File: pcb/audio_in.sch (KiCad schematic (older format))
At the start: 18 parts, among them U7 MCP6409

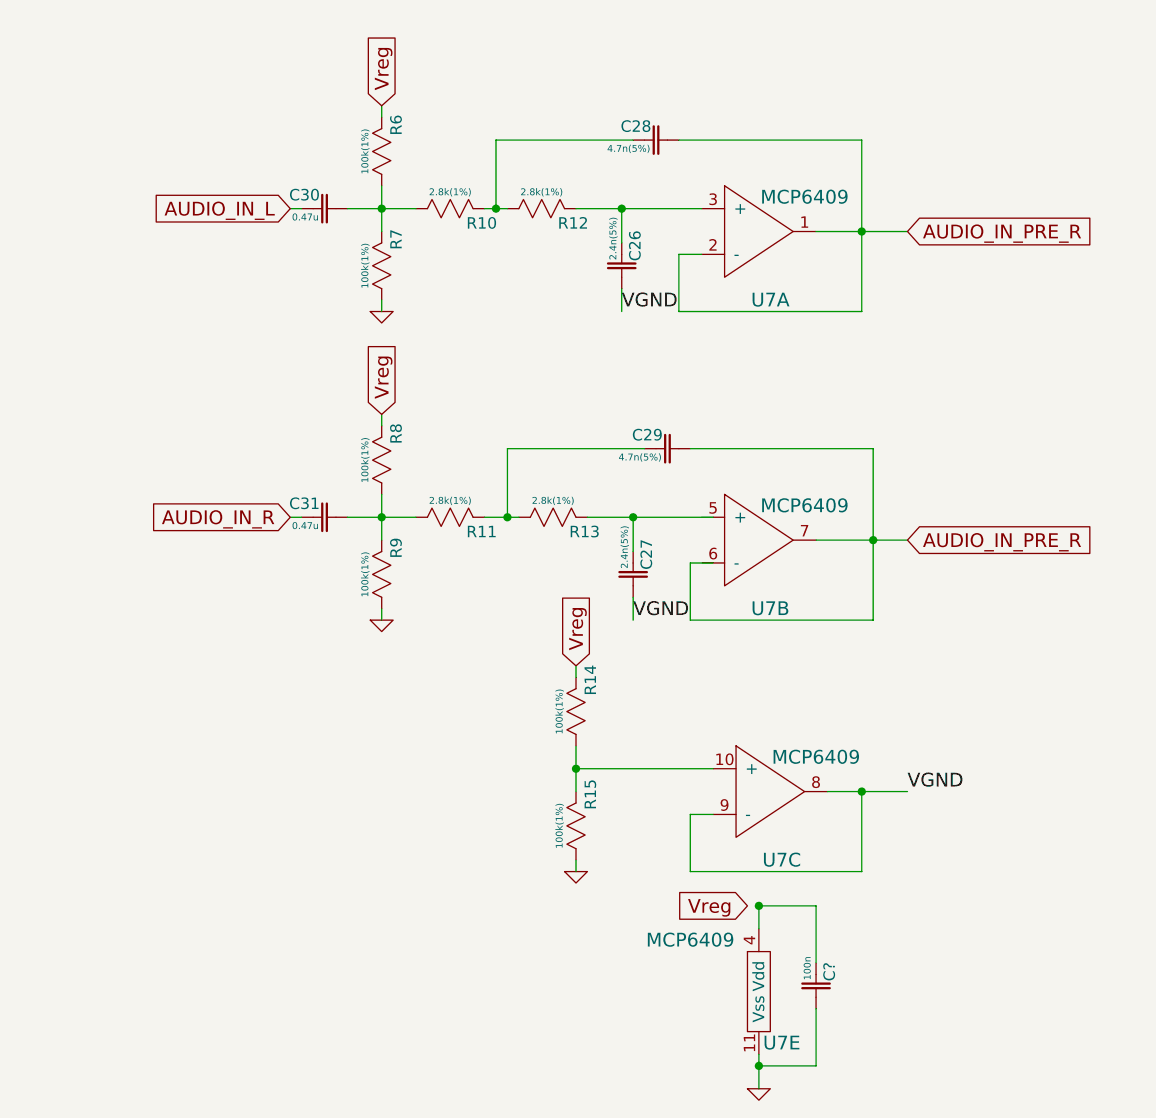
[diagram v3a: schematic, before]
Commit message: Added TRS audio connector
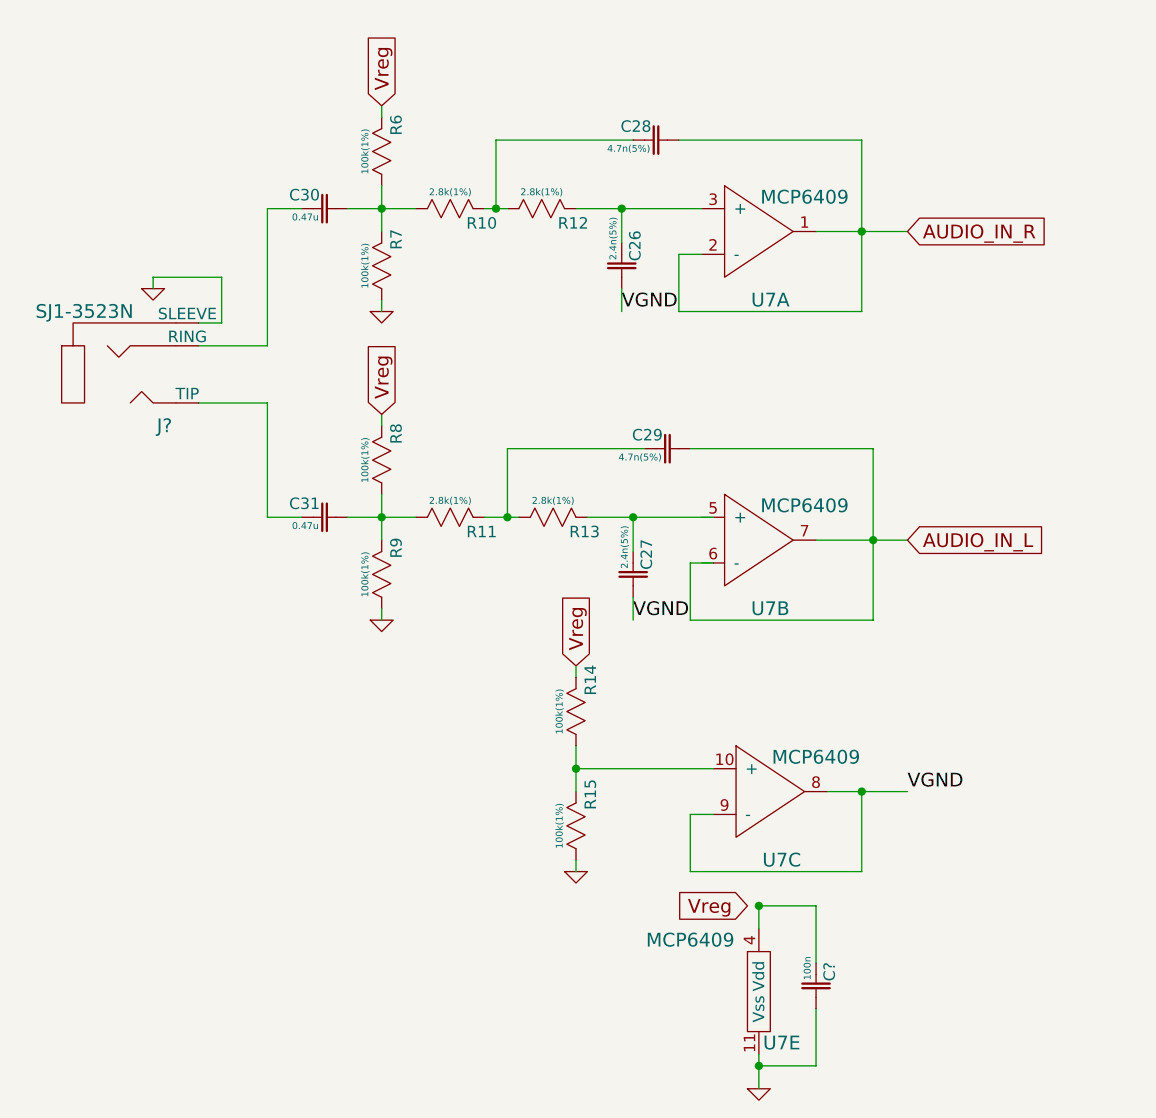
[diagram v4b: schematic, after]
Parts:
- added J?: SJ1-3523N, symbol TRS_CONN
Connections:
- net labels removed: AUDIO_IN_PRE_R
- wire segments 49 -> 57
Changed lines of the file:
@@
-EESchema Schematic File Version 2  date Thu 26 Jul 2012 02:13:26 PM EDT
+EESchema Schematic File Version 2  date Thu 26 Jul 2012 02:28:43 PM EDT
 LIBS:power
 LIBS:device
@@
 $EndDescr
 Wire Wire Line
+	1700 4000 1550 4000
+Wire Wire Line
+	1550 4000 1550 3500
+Wire Wire Line
+	1550 3500 1250 3500
+Wire Wire Line
+	1250 3150 1350 3150
+Wire Wire Line
+	1350 3150 1350 2950
+Wire Wire Line
+	1350 2950 1050 2950
+Wire Wire Line
+	1050 2950 1050 3000
+Wire Wire Line
+	3700 6400 3950 6400
+Connection ~ 3700 6400
+Wire Wire Line
+	3950 6400 3950 6150
+Connection ~ 3700 5700
+Wire Wire Line
+	3950 5950 3950 5700
+Wire Wire Line
+	1900 4000 2200 4000
+Wire Wire Line
+	2050 3550 2050 3600
+Wire Wire Line
+	2050 4450 2050 4400
+Connection ~ 2050 4000
+Wire Wire Line
+	2050 3900 2050 4100
+Wire Wire Line
+	3150 4350 3150 4450
+Wire Wire Line
+	3100 3100 3100 3000
+Connection ~ 4150 5200
+Wire Wire Line
+	4000 5200 4350 5200
+Wire Wire Line
+	4150 5200 4150 5550
+Wire Wire Line
+	4150 5550 3400 5550
+Wire Wire Line
+	3400 5550 3400 5300
+Wire Wire Line
+	3400 5300 3500 5300
+Wire Wire Line
+	2900 4650 2900 4700
+Connection ~ 4200 4100
+Wire Wire Line
+	3950 4100 4350 4100
+Wire Wire Line
+	4200 4450 4200 3700
+Wire Wire Line
+	4200 4450 3400 4450
+Wire Wire Line
+	3400 4450 3400 4200
+Wire Wire Line
+	3400 4200 3500 4200
+Wire Wire Line
+	2900 5550 2900 5500
+Connection ~ 2600 4000
+Wire Wire Line
+	2500 4000 2650 4000
+Connection ~ 3150 4000
+Wire Wire Line
+	3150 4000 3150 4150
+Wire Wire Line
+	2950 4000 3500 4000
+Wire Wire Line
+	4200 3700 3400 3700
+Wire Wire Line
+	3200 3700 2600 3700
+Wire Wire Line
+	2600 3700 2600 4000
+Connection ~ 2900 5100
+Wire Wire Line
+	2900 5100 3500 5100
+Wire Wire Line
+	2900 5000 2900 5200
+Connection ~ 4150 2750
+Wire Wire Line
+	3350 3100 4150 3100
+Wire Wire Line
+	3350 3100 3350 2850
+Wire Wire Line
+	3350 2850 3450 2850
+Wire Wire Line
+	2050 3100 2050 3050
+Connection ~ 2550 2650
+Wire Wire Line
+	2500 2650 2600 2650
+Connection ~ 3100 2650
+Wire Wire Line
+	3100 2650 3100 2800
+Wire Wire Line
+	2900 2650 3450 2650
+Wire Wire Line
+	3950 2750 4350 2750
+Wire Wire Line
+	4150 3100 4150 2350
+Wire Wire Line
+	4150 2350 3350 2350
+Wire Wire Line
+	3150 2350 2550 2350
+Wire Wire Line
+	2550 2350 2550 2650
+Wire Wire Line
+	2050 2200 2050 2250
+Connection ~ 2050 2650
+Wire Wire Line
+	1900 2650 2200 2650
+Wire Wire Line
+	2050 2550 2050 2750
+Wire Wire Line
+	3700 6500 3700 6350
+Wire Wire Line
+	3700 5800 3700 5700
+Wire Wire Line
 	3700 5700 3950 5700
 Wire Wire Line
-	3700 5700 3700 5800
-Wire Wire Line
-	3700 6500 3700 6350
-Wire Wire Line
-	2050 2550 2050 2750
-Wire Wire Line
-	1900 2650 2200 2650
-Connection ~ 2050 2650
-Wire Wire Line
-	2050 2200 2050 2250
-Wire Wire Line
-	2550 2650 2550 2350
-Wire Wire Line
-	2550 2350 3150 2350
-Wire Wire Line
-	3350 2350 4150 2350
-Wire Wire Line
-	4150 2350 4150 3100
-Wire Wire Line
-	3950 2750 4350 2750
-Wire Wire Line
-	2900 2650 3450 2650
-Wire Wire Line
-	3100 2650 3100 2800
-Connection ~ 3100 2650
-Wire Wire Line
-	2500 2650 2600 2650
-Connection ~ 2550 2650
-Wire Wire Line
-	2050 3100 2050 3050
-Wire Wire Line
-	3450 2850 3350 2850
-Wire Wire Line
-	3350 2850 3350 3100
-Wire Wire Line
-	3350 3100 4150 3100
-Connection ~ 4150 2750
-Wire Wire Line
-	2900 5000 2900 5200
-Wire Wire Line
-	2900 5100 3500 5100
-Connection ~ 2900 5100
-Wire Wire Line
-	2600 4000 2600 3700
-Wire Wire Line
-	2600 3700 3200 3700
-Wire Wire Line
-	3400 3700 4200 3700
-Wire Wire Line
-	2950 4000 3500 4000
-Wire Wire Line
-	3150 4000 3150 4150
-Connection ~ 3150 4000
-Wire Wire Line
-	2500 4000 2650 4000
-Connection ~ 2600 4000
-Wire Wire Line
-	2900 5550 2900 5500
-Wire Wire Line
-	3500 4200 3400 4200
-Wire Wire Line
-	3400 4200 3400 4450
-Wire Wire Line
-	3400 4450 4200 4450
-Wire Wire Line
-	4200 4450 4200 3700
-Wire Wire Line
-	3950 4100 4350 4100
-Connection ~ 4200 4100
-Wire Wire Line
-	2900 4650 2900 4700
-Wire Wire Line
-	3500 5300 3400 5300
-Wire Wire Line
-	3400 5300 3400 5550
-Wire Wire Line
-	3400 5550 4150 5550
-Wire Wire Line
-	4150 5550 4150 5200
-Wire Wire Line
-	4000 5200 4350 5200
-Connection ~ 4150 5200
-Wire Wire Line
-	3100 3100 3100 3000
-Wire Wire Line
-	3150 4350 3150 4450
-Wire Wire Line
-	2050 3900 2050 4100
-Connection ~ 2050 4000
-Wire Wire Line
-	2050 4450 2050 4400
-Wire Wire Line
-	2050 3550 2050 3600
-Wire Wire Line
-	1900 4000 2200 4000
-Wire Wire Line
-	1650 2650 1700 2650
-Wire Wire Line
-	1700 4000 1650 4000
-Wire Wire Line
-	3950 5700 3950 5950
-Connection ~ 3700 5700
-Wire Wire Line
-	3950 6150 3950 6400
-Connection ~ 3700 6400
-Wire Wire Line
-	3950 6400 3700 6400
+	1250 3250 1550 3250
+Wire Wire Line
+	1550 3250 1550 2650
+Wire Wire Line
+	1550 2650 1700 2650
+$Comp
+L GND #PWR?
+U 1 1 50118BD6
+P 1050 3000
+F 0 "#PWR?" H 1050 3000 30  0001 C CNN
+F 1 "GND" H 1050 2930 30  0001 C CNN
+	1    1050 3000
+	1    0    0    -1
+$EndComp
+$Comp
+L TRS_CONN J?
+U 1 1 50118BBE
+P 800 3350
+F 0 "J?" H 1100 3100 60  0000 C CNN
+F 1 "SJ1-3523N" H 750 3600 60  0000 C CNN
+	1    800  3350
+	1    0    0    -1
+$EndComp
 $Comp
 L CAP C?
@@
 	1    0    0    -1
 $EndComp
-Text GLabel 1650 2650 0    60   Input ~ 0
+Text GLabel 4350 4100 2    60   Input ~ 0
 AUDIO_IN_L
-Text GLabel 1650 4000 0    60   Input ~ 0
+Text GLabel 4350 2750 2    60   Input ~ 0
 AUDIO_IN_R
-Text GLabel 4350 4100 2    60   Input ~ 0
-AUDIO_IN_PRE_R
-Text GLabel 4350 2750 2    60   Input ~ 0
-AUDIO_IN_PRE_R
 $Comp
 L CAP C30

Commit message: Added LCD and started wiring busses
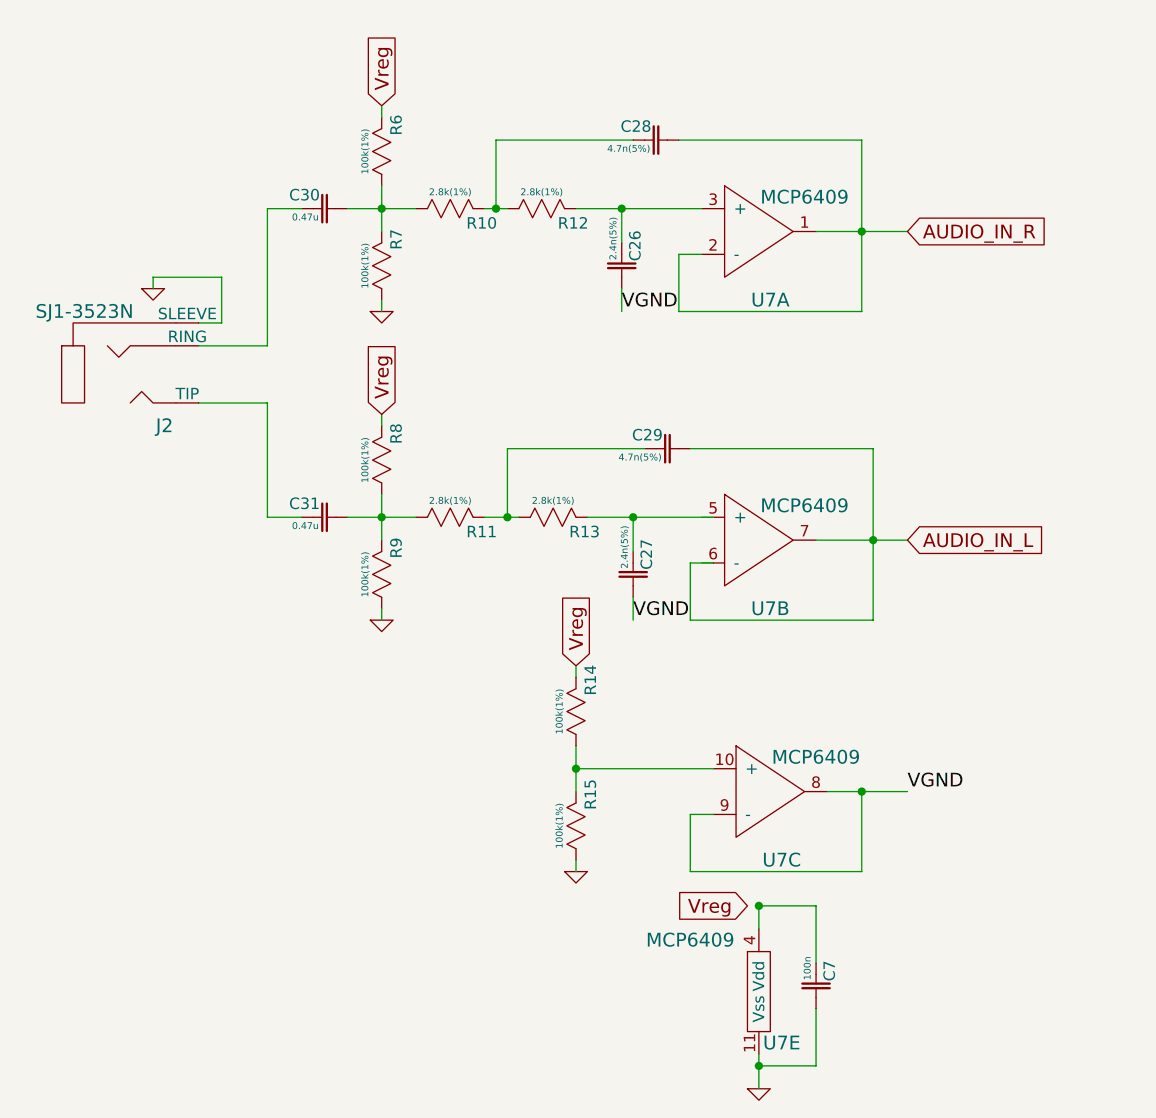
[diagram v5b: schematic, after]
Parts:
- gave numbers to parts that had none: 2
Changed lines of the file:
@@
-EESchema Schematic File Version 2  date Thu 26 Jul 2012 02:28:43 PM EDT
+EESchema Schematic File Version 2  date Thu 26 Jul 2012 11:54:13 PM EDT
 LIBS:power
 LIBS:device
@@
 EELAYER 25  0
 EELAYER END
-$Descr A4 11700 8267
+$Descr A4 11693 8268
 encoding utf-8
 Sheet 5 5
 Title ""
-Date "26 jul 2012"
+Date "27 jul 2012"
 Rev ""
 Comp ""
@@
 	1550 2650 1700 2650
 $Comp
-L GND #PWR?
+L GND #PWR24
 U 1 1 50118BD6
 P 1050 3000
-F 0 "#PWR?" H 1050 3000 30  0001 C CNN
+F 0 "#PWR24" H 1050 3000 30  0001 C CNN
 F 1 "GND" H 1050 2930 30  0001 C CNN
 	1    1050 3000
@@
 $EndComp
 $Comp
-L TRS_CONN J?
+L TRS_CONN J2
 U 1 1 50118BBE
 P 800 3350
-F 0 "J?" H 1100 3100 60  0000 C CNN
+F 0 "J2" H 1100 3100 60  0000 C CNN
 F 1 "SJ1-3523N" H 750 3600 60  0000 C CNN
 	1    800  3350
@@
 $EndComp
 $Comp
-L CAP C?
+L CAP C7
 U 1 1 50118878
 P 3950 6050
-F 0 "C?" H 3970 6020 50  0000 L TNN
+F 0 "C7" H 3970 6020 50  0000 L TNN
 F 1 "100n" H 3975 6070 30  0000 L BNN
 	1    3950 6050
@@
 Vreg
 $Comp
-L GND #PWR25
+L GND #PWR28
 U 1 1 5010D90D
 P 3700 6500
-F 0 "#PWR25" H 3700 6500 30  0001 C CNN
+F 0 "#PWR28" H 3700 6500 30  0001 C CNN
 F 1 "GND" H 3700 6430 30  0001 C CNN
 	1    3700 6500
@@
 Vreg
 $Comp
-L GND #PWR22
+L GND #PWR25
 U 1 1 5010D9BD
 P 2050 3100
-F 0 "#PWR22" H 2050 3100 30  0001 C CNN
+F 0 "#PWR25" H 2050 3100 30  0001 C CNN
 F 1 "GND" H 2050 3030 30  0001 C CNN
 	1    2050 3100
@@
 Vreg
 $Comp
-L GND #PWR24
+L GND #PWR27
 U 1 1 5010DA28
 P 2900 5550
-F 0 "#PWR24" H 2900 5550 30  0001 C CNN
+F 0 "#PWR27" H 2900 5550 30  0001 C CNN
 F 1 "GND" H 2900 5480 30  0001 C CNN
 	1    2900 5550
@@
 Vreg
 $Comp
-L GND #PWR23
+L GND #PWR26
 U 1 1 5010DC3F
 P 2050 4450
-F 0 "#PWR23" H 2050 4450 30  0001 C CNN
+F 0 "#PWR26" H 2050 4450 30  0001 C CNN
 F 1 "GND" H 2050 4380 30  0001 C CNN
 	1    2050 4450

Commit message: Broke up schematic in a more modular fashion -- Added LCD footprint
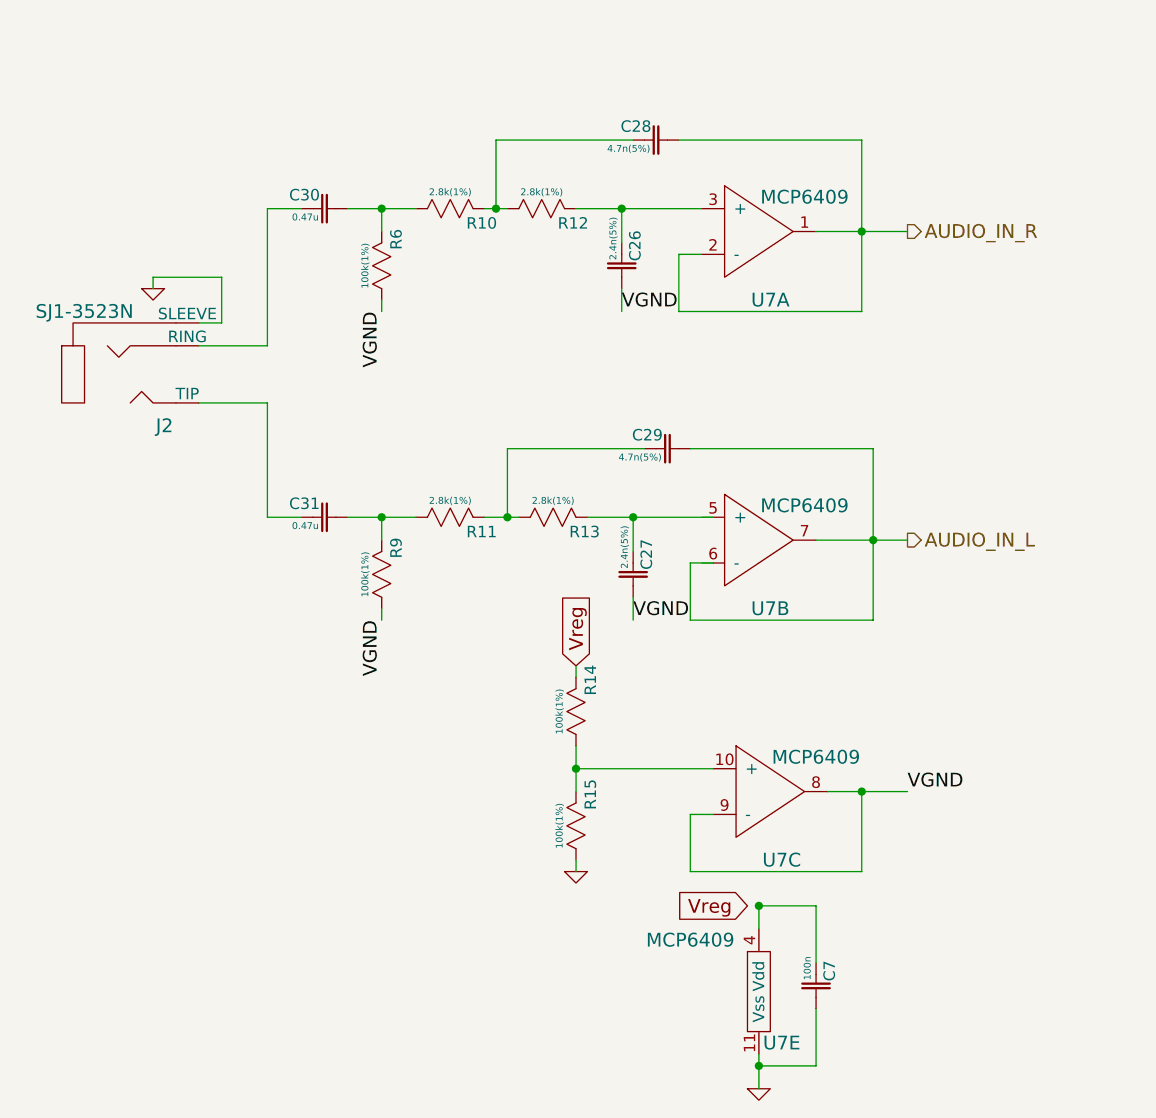
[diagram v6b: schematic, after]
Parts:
- removed R7, R8: 100k(1%), symbol RES
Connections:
- wire segments 57 -> 55
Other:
- moved on the sheet: R6
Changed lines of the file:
@@
-EESchema Schematic File Version 2  date Thu 26 Jul 2012 11:54:13 PM EDT
+EESchema Schematic File Version 2  date Tue 31 Jul 2012 10:29:35 PM EDT
 LIBS:power
 LIBS:device
@@
 EELAYER 25  0
 EELAYER END
-$Descr A4 11693 8268
+$Descr A4 11700 8267
 encoding utf-8
-Sheet 5 5
+Sheet 6 6
 Title ""
-Date "27 jul 2012"
+Date "1 aug 2012"
 Rev ""
 Comp ""
@@
 Comment4 ""
 $EndDescr
+Text HLabel 4350 4100 2    60   Output ~ 0
+AUDIO_IN_L
+Text HLabel 4350 2750 2    60   Output ~ 0
+AUDIO_IN_R
+Wire Wire Line
+	2050 4000 2050 4100
+Wire Wire Line
+	2050 3100 2050 3050
 Wire Wire Line
 	1700 4000 1550 4000
@@
 	1900 4000 2200 4000
 Wire Wire Line
-	2050 3550 2050 3600
-Wire Wire Line
 	2050 4450 2050 4400
 Connection ~ 2050 4000
 Wire Wire Line
-	2050 3900 2050 4100
-Wire Wire Line
 	3150 4350 3150 4450
 Wire Wire Line
@@
 Wire Wire Line
 	3350 2850 3450 2850
-Wire Wire Line
-	2050 3100 2050 3050
 Connection ~ 2550 2650
 Wire Wire Line
@@
 Wire Wire Line
 	2550 2350 2550 2650
-Wire Wire Line
-	2050 2200 2050 2250
 Connection ~ 2050 2650
 Wire Wire Line
 	1900 2650 2200 2650
 Wire Wire Line
-	2050 2550 2050 2750
-Wire Wire Line
 	3700 6500 3700 6350
 Wire Wire Line
@@
 Wire Wire Line
 	1550 2650 1700 2650
-$Comp
-L GND #PWR24
+Wire Wire Line
+	2050 2750 2050 2650
+Text Label 2050 4450 3    60   ~ 0
+VGND
+Text Label 2050 3100 3    60   ~ 0
+VGND
+$Comp
+L GND #PWR026
 U 1 1 50118BD6
 P 1050 3000
-F 0 "#PWR24" H 1050 3000 30  0001 C CNN
+F 0 "#PWR026" H 1050 3000 30  0001 C CNN
 F 1 "GND" H 1050 2930 30  0001 C CNN
 	1    1050 3000
@@
 Vreg
 $Comp
-L GND #PWR28
+L GND #PWR027
 U 1 1 5010D90D
 P 3700 6500
-F 0 "#PWR28" H 3700 6500 30  0001 C CNN
+F 0 "#PWR027" H 3700 6500 30  0001 C CNN
 F 1 "GND" H 3700 6430 30  0001 C CNN
 	1    3700 6500
@@
 L RES R6
 U 1 1 5010D932
-P 2050 2400
-F 0 "R6" H 2120 2365 50  0000 L TNN
-F 1 "100k(1%)" H 2050 2455 30  0000 C BNN
-	1    2050 2400
-	0    -1   -1   0
-$EndComp
-$Comp
-L RES R7
-U 1 1 5010D938
 P 2050 2900
-F 0 "R7" H 2120 2865 50  0000 L TNN
+F 0 "R6" H 2120 2865 50  0000 L TNN
 F 1 "100k(1%)" H 2050 2955 30  0000 C BNN
 	1    2050 2900
@@
 	-1   0    0    1
 $EndComp
-Text GLabel 2050 2200 1    60   Input ~ 0
-Vreg
-$Comp
-L GND #PWR25
-U 1 1 5010D9BD
-P 2050 3100
-F 0 "#PWR25" H 2050 3100 30  0001 C CNN
-F 1 "GND" H 2050 3030 30  0001 C CNN
-	1    2050 3100
-	1    0    0    -1
-$EndComp
 $Comp
 L RES R13
@@
 Vreg
 $Comp
-L GND #PWR27
+L GND #PWR028
 U 1 1 5010DA28
 P 2900 5550
-F 0 "#PWR27" H 2900 5550 30  0001 C CNN
+F 0 "#PWR028" H 2900 5550 30  0001 C CNN
 F 1 "GND" H 2900 5480 30  0001 C CNN
 	1    2900 5550
@@
 Text Label 3100 3100 0    60   ~ 0
 VGND
-$Comp
-L RES R8
-U 1 1 5010DC2F
-P 2050 3750
-F 0 "R8" H 2120 3715 50  0000 L TNN
-F 1 "100k(1%)" H 2050 3805 30  0000 C BNN
-	1    2050 3750
-	0    -1   -1   0
-$EndComp
 $Comp
 L RES R9
@@
 	0    -1   -1   0
 $EndComp
-Text GLabel 2050 3550 1    60   Input ~ 0
-Vreg
-$Comp
-L GND #PWR26
-U 1 1 5010DC3F
-P 2050 4450
-F 0 "#PWR26" H 2050 4450 30  0001 C CNN
-F 1 "GND" H 2050 4380 30  0001 C CNN
-	1    2050 4450
-	1    0    0    -1
-$EndComp
 $Comp
 L RES R11
@@
 	1    0    0    -1
 $EndComp
-Text GLabel 4350 4100 2    60   Input ~ 0
-AUDIO_IN_L
-Text GLabel 4350 2750 2    60   Input ~ 0
-AUDIO_IN_R
 $Comp
 L CAP C30
